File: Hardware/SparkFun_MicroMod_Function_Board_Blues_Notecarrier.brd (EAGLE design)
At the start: 160 x 100 mm, 3 parts, among them J1 MICROMOD_FUNCTION_STANDARD, U1 NOTECARD

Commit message: Board nearly complete, nearing readiness for design review.
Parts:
- added ANT_PWR, WP: JUMPER-SMT_2_NO_SILK, SparkFun-Jumpers:SMT-JUMPER_2_NO_SILK
- added AUX_EN_LED, USB_SHLD, VIO_LED, VMODEM_LED: JUMPER-SMT_2_NC_TRACE_SILK, SparkFun-Jumpers:SMT-JUMPER_2_NC_TRACE_SILK
- added C1, C5, C6, C7: 0.1uF, SparkFun-Capacitors:0402-TIGHT
- added C2: 10uF, SparkFun-Capacitors:0805
- added C3, C4: 100uF, SparkFun-Capacitors:PANASONIC_D
- added C8: 1.0uF, SparkFun-Capacitors:0402-TIGHT
- added D1, D2: RED, SparkFun-LED:LED-0603
- added D3: BLUE, SparkFun-LED:LED-0603
- added D4: PRTR5V0U2F, SparkFun-IC-Power:SOT886
- added D5, D6: 3A/10V/280mV, SparkFun-DiscreteSemi:SOD-323
- added D7: 0.5A/40V/420mV, SparkFun-DiscreteSemi:SOD-323
- added FD1, FD2, FD3, FD4: FIDUCIALUFIDUCIAL, SparkFun-Aesthetics:FIDUCIAL-MICRO
- added H1: STAND-OFF-REFLOW-M2.5_2.5MM_TALL, SparkFun-Hardware:STAND-OFF-REFLOW-M2.5
- added J2: MICROMOD_FUNCTION_STANDARD, SparkFun-MicroMod:M.2-CARD-E-22_FUNCTION_STANDARD
- added J3: (no value), SparkFun-Connectors:1X01_NO_SILK
- added J4: (no value), SparkFun-Connectors:1X07_NO_SILK
- added J5: (no value), SparkFun-Connectors:NANO_SIM_MOLEX_104224-0820
- added J6: NOTECARD, SparkFun_MicroMod_Function_Board_Blues_Notecarrier:M.2-CONNECTOR-E
- added LOGO1: SFE_LOGO_NAME_FLAME.1_INCH, SparkFun-Aesthetics:SFE_LOGO_NAME_FLAME_.1
- added LOGO2: SPECIAL_INSTRUCTIONS-ORDERING, SparkFun-Aesthetics:ORDERING_INSTRUCTIONS
- added LOGO3: OSHW-LOGOMINI, SparkFun-Aesthetics:OSHW-LOGO-MINI
- added MEAS: JUMPER-COMBO_2_NC_TRACE, SparkFun-Jumpers:COMBO-JUMPER_2_NC_TRACE
- added Q1, Q3: 5.8A/30V/35mΩ, SparkFun-DiscreteSemi:SOT23-3
- added Q2, Q4: 20V/4.2A/52mΩ/1.4W, SparkFun-DiscreteSemi:SOT23-3
- added R1, R2: 1k, SparkFun-Resistors:0402-TIGHT
- added R10, R11, R13, R5, R7, R9: 10k, SparkFun-Resistors:0402-TIGHT
- added R12: 2.2M, SparkFun-Resistors:0402-TIGHT
- added R3, R4: 5.1k, SparkFun-Resistors:0402-TIGHT
- added R6: 4.7k, SparkFun-Resistors:0402-TIGHT
- added R8: 560Ω, SparkFun-Resistors:0402-TIGHT
- added S1: MOMENTARY-SWITCH-SPST-SMD-4.6X2.8MM, SparkFun-Switches:TACTILE_SWITCH_SMD_4.6X2.8MM
- added U$1: (no value), output:AEN1
- added U$10: (no value), output:#_AUX3#MCU_#BOOT##0
- added U$11: (no value), output:#_AUX2#0
- added U$12: (no value), output:#_MCU_#DFU_STAT##0
- added U$13: (no value), output:#_AUX_EN#0
- added U$14: (no value), SparkFun-Aesthetics:SFE_LOGO_NAME_FLAME_.1
- added U$15: (no value), output:BLUES_WIRELESS_NOTECARRIER1
- added U$2: (no value), output:VIN3
- added U$3: (no value), output:VIO4
- added U$4: (no value), output:##RESET_##6
- added U$5: (no value), output:##RESET##9
- added U$6: (no value), SparkFun-Aesthetics:SFE_LOGO_FLAME_STOP_.1
- added U$7: (no value), output:#_GND_#0
- added U$8: (no value), output:#_AUX5#0
- added U$9: (no value), output:#_AUX4#MCU_#RST##0
- added U2: TCR2EF33, SparkFun_MicroMod_Function_Board_Blues_Notecarrier:SOT23-5
- J1: value MICROMOD_FUNCTION_STANDARD -> (none); device SparkFun-MicroMod:M.2-CARD-E-22_FUNCTION_STANDARD -> SparkFun-Connectors:USB-C-16P-2LAYER-PADS
- U1: value NOTECARD -> EEPROM; device SparkFun_MicroMod_Function_Board_Blues_Notecarrier:M.2-CONNECTOR-E -> SparkFun-IC-Memory:SO08
- moved J1 108.2 mm to (30.0, 58.9), turned to 180 degrees
- moved U1 55.2 mm to (34.0, 8.70)
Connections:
- new net !RESET!: J3.1, J6.67, S1.3, S1.4
- new net 3.3V: C1.1, C7.1, D1.A, D7.C, J6.2, J6.4, Q2.3, R10.1, R5.1, U1.8
- new net 3V3_IN: J2.73, Q2.2, R7.1, R9.2
- new net A0: J2.36, U1.1
- new net A1: J2.34, U1.2
- new net A2: J2.32, U1.3
- new net ATTN: J2.53, J6.54
- new net AUX1/MCU_!DFU_STAT!: J2.10, J4.6, J6.46
- new net AUX2: J2.57, J4.5, J6.48
- new net AUX3/MCU_!BOOT!: J2.66, J4.4, J6.50
- new net AUX4/MCU_!RST!: J2.68, J4.3, J6.52
- new net AUX5: J2.59, J4.7, J6.38
- new net AUX_EN: D3.A, J2.55, J4.2, J6.56, R10.2
- new net AUX_RX/MCU_TX: J2.4, J6.58
- new net AUX_TX/MCU_RX: J2.6, J6.60
- new net EWP: J2.40, R5.2, U1.7, WP.2
- new net GND: AUX_EN_LED.1, C1.2, C2.2, C3.-, C4.-, C5.2, C6.2, C7.2, C8.2, D4.2, H1.1, J1.GND, J1.GND2, J2.1, J2.2, J2.33, J2.39, J2.45, J2.75, J2.8, J2.GND1, J2.GND2, J2.GND3, J2.GND4, J2.GND5, J2.GND6, J4.1, J5.G1, J5.G2, J5.G3, J5.G4, J5.S4, J6.11, J6.18, J6.3, J6.33, J6.39, J6.45, J6.5, J6.51, J6.57, J6.6, J6.71, J6.73, Q1.2, Q3.2, R12.1, R3.1, R4.1, S1.1, S1.2, U1.4, U2.2, USB_SHLD.1, VIO_LED.1, VMODEM_LED.1, WP.1
- new net N$1: J2.71, R8.2
- new net N$10: C8.1, D7.A, U2.5
- new net N$11: R2.1, VMODEM_LED.2
- new net N$12: R1.1, VIO_LED.2
- new net N$13: D3.C, R6.2
- new net N$14: AUX_EN_LED.2, R6.1
- new net N$2: Q1.3, Q2.1, R9.1
- new net N$3: Q3.3, Q4.1, R11.1
- new net N$37: D5.C, D6.C, MEAS.1, MEAS.3
- new net N$4: D1.C, R1.2
- new net N$5: R13.1, U2.3
- new net N$6: D2.C, R2.2
- new net N$8: J1.B5, R3.2
- new net N$9: J1.A5, R4.2
- new net NOTECARD_RX: J2.13, J6.62
- new net NOTECARD_TX: J2.15, J6.64
- new net PWR_EN: Q1.1, Q3.1, R7.2, R8.1
- new net SCL: J2.21, J6.40, U1.6
- new net SDA: J2.19, J6.42, U1.5
- new net SHLD: J1.SHLD1, J1.SHLD2, J1.SHLD3, J1.SHLD4, USB_SHLD.2
- new net SIM_CLK: J5.S3, J6.14
- new net SIM_IO: J5.S6, J6.12
- new net SIM_RST: J5.S2, J6.10
- new net SIM_VCC: C2.1, J5.S1, J6.8
- new net USB_IN_N: D4.3, J1.A7, J1.B7
- new net USB_IN_P: D4.1, J1.A6, J1.B6
- new net USB_N: D4.4, J6.9
- new net USB_P: D4.6, J6.7
- new net VACT_GPS_IN: ANT_PWR.2, J6.22
- new net VACT_GPS_OUT: ANT_PWR.1, J6.20
- new net VCC: D6.A, Q4.3
- new net VCC_IN: J2.72, J2.74, Q4.2, R11.2
- new net VIN: C3.+, C4.+, C6.1, D2.A, J6.70, J6.72, J6.74, MEAS.2, MEAS.4, R12.2
- new net V_USB: C5.1, D4.5, D5.A, J1.VBUS1, J1.VBUS2, J6.13, R13.2, U2.1
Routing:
- net AUX_EN: track 0.00 -> 97.7 mm, vias 0 -> 7
- net 3.3V: track 0.00 -> 66.9 mm, vias 0 -> 2
- net AUX5: track 0.00 -> 62.0 mm, vias 0 -> 2
- net VIN: track 0.00 -> 57.2 mm, vias 0 -> 2
- net AUX1/MCU_!DFU_STAT!: track 0.00 -> 57.2 mm, vias 0 -> 1
- net !RESET!: track 0.00 -> 56.1 mm, vias 0 -> 1
- net SIM_RST: track 0.00 -> 55.8 mm, vias 0 -> 2
- net AUX2: track 0.00 -> 53.0 mm, vias 0 -> 2
- net AUX3/MCU_!BOOT!: track 0.00 -> 50.0 mm, vias 0 -> 1
- net SIM_CLK: track 0.00 -> 49.0 mm
- net AUX4/MCU_!RST!: track 0.00 -> 47.3 mm, vias 0 -> 1
- net SIM_IO: track 0.00 -> 46.3 mm
- net USB_N: track 0.00 -> 45.1 mm, vias 0 -> 2
- net USB_P: track 0.00 -> 45.0 mm, vias 0 -> 2
- net SDA: track 0.00 -> 43.7 mm, vias 0 -> 3
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- added copper zone on layer 1, net 3.3V
- added copper zone on layer 1, net GND
- added copper zone on layer 16, net GND
- added copper zone on layer 1, net SHLD
- added copper zone on layer 16, net SHLD
- added copper zone on layer 1, net SIM_VCC
- added copper zone on layer 16, net SIM_VCC
- added copper zone on layer 1, net VCC_IN
- added copper zone on layer 16, net VCC_IN
- added copper zone on layer 1, net VIN
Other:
- board size 160 x 100 mm -> 37.5 x 65 mm
- board text added: "Alex Brudner"
- board text added: "v01"

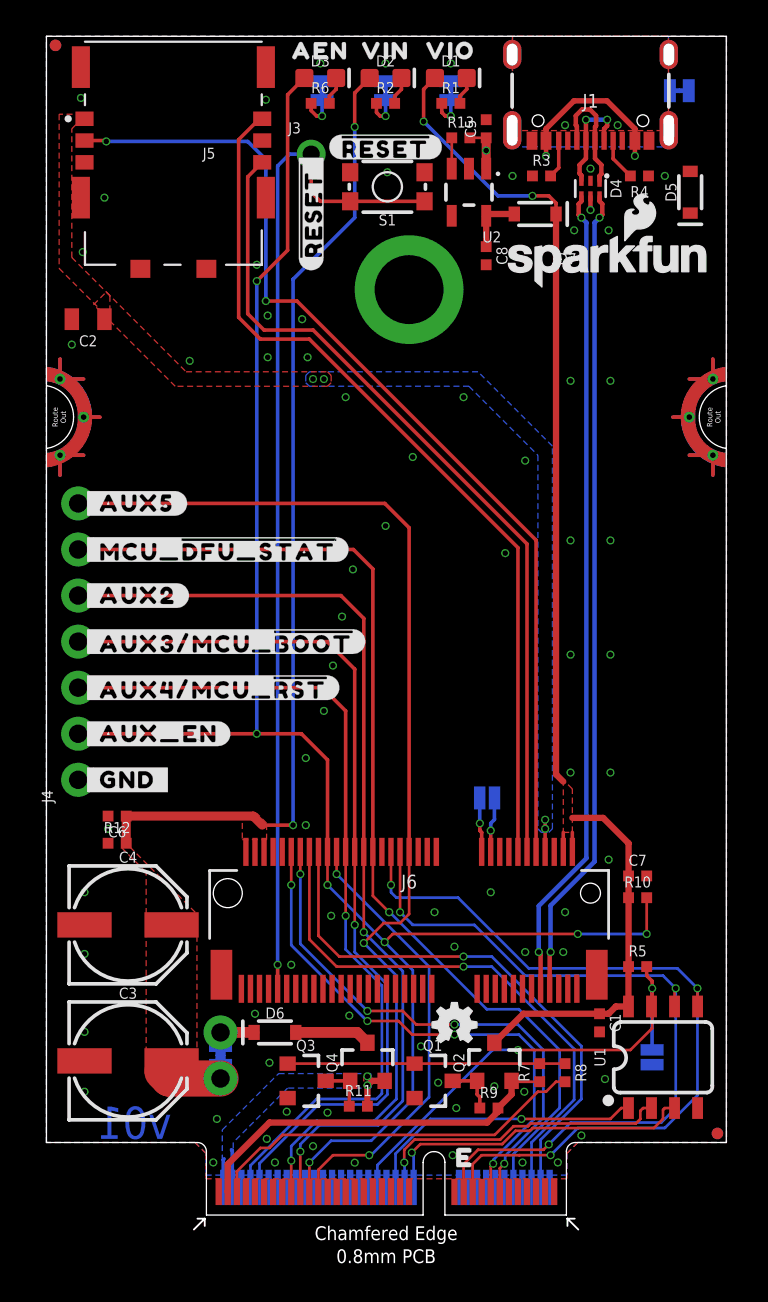
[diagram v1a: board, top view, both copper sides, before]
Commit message: Board routing complete.
Initial routing complete, now finishing silk.
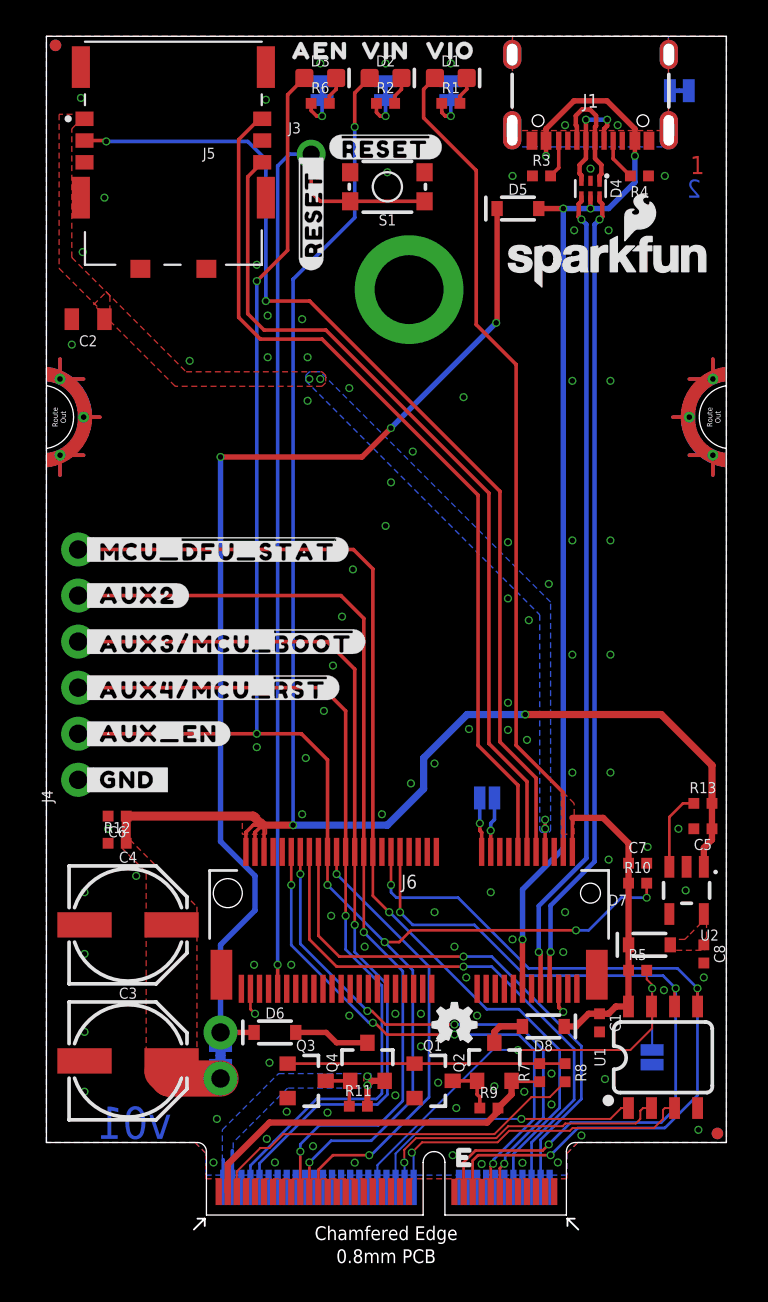
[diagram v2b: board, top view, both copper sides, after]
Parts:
- removed U$8: (no value), output:#_AUX5#0
- added D8: 0.5A/40V/420mV, SparkFun-DiscreteSemi:SOD-323
- J4: device SparkFun-Connectors:1X07_NO_SILK -> SparkFun-Connectors:1X06_NO_SILK
- moved D7 40.8 mm to (33.2, 14.9), turned to 0 degrees
- moved C5 40.4 mm to (36.2, 21.3), turned to 180 degrees
- moved C8 40.3 mm to (36.2, 14.4)
- moved U2 40.3 mm to (35.3, 17.9)
- moved R13 39.1 mm to (36.2, 22.7)
- moved D5 9.54 mm to (26.0, 55.5), turned to 0 degrees
- moved R10 0.80 mm to (32.6, 18.3)
- moved C7 0.70 mm to (32.6, 19.4)
- moved R5 0.20 mm to (32.6, 13.5)
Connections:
- removed net AUX5: J2.59, J4.7, J6.38
- new net N$7: D8.A, Q2.3
- net 3.3V: now also D8.C; no longer Q2.3
- net VIN: now also C5.1, R13.2, U2.1
- net V_USB: no longer C5.1, R13.2, U2.1
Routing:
- net AUX5: track 62.0 -> 0.00 mm, vias 2 -> 0
- net N$37: track 1.85 -> 60.5 mm, vias 0 -> 3
- net V_USB: track 12.5 -> 61.2 mm, vias 4 -> 5
- net VIN: track 57.2 -> 96.8 mm, vias 2 -> 3
- net N$10: track 3.29 -> 0.00 mm
- net GND: track 0.00 -> 2.86 mm, vias 17 -> 105
- net N$5: track 1.70 -> 4.41 mm
- net N$7: track 0.00 -> 2.27 mm
- net 3.3V: track 66.9 -> 64.7 mm, vias 2 -> 0
- added copper zone on layer 1, net N$10
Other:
- board text added: "1"
- board text added: "2"

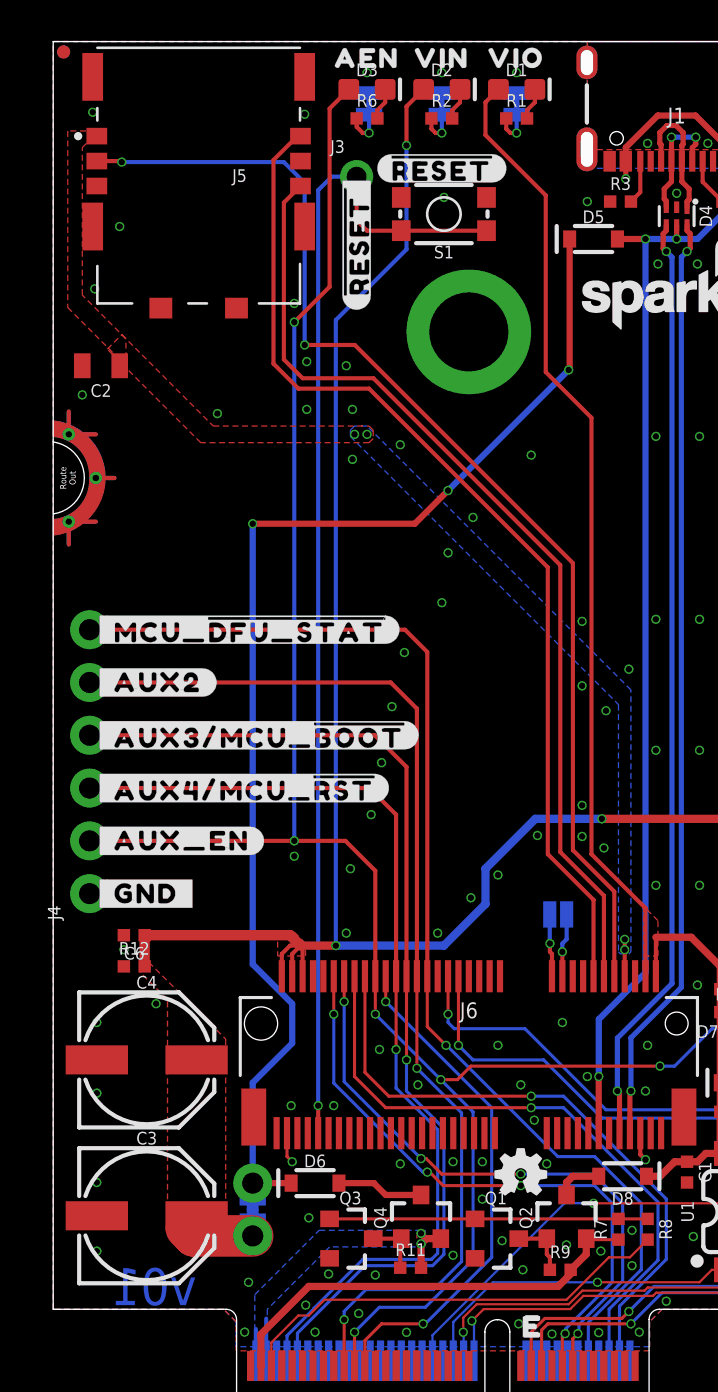
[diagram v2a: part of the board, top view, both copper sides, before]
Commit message: Initial Silk completed.
May add Blues Wireless logo.
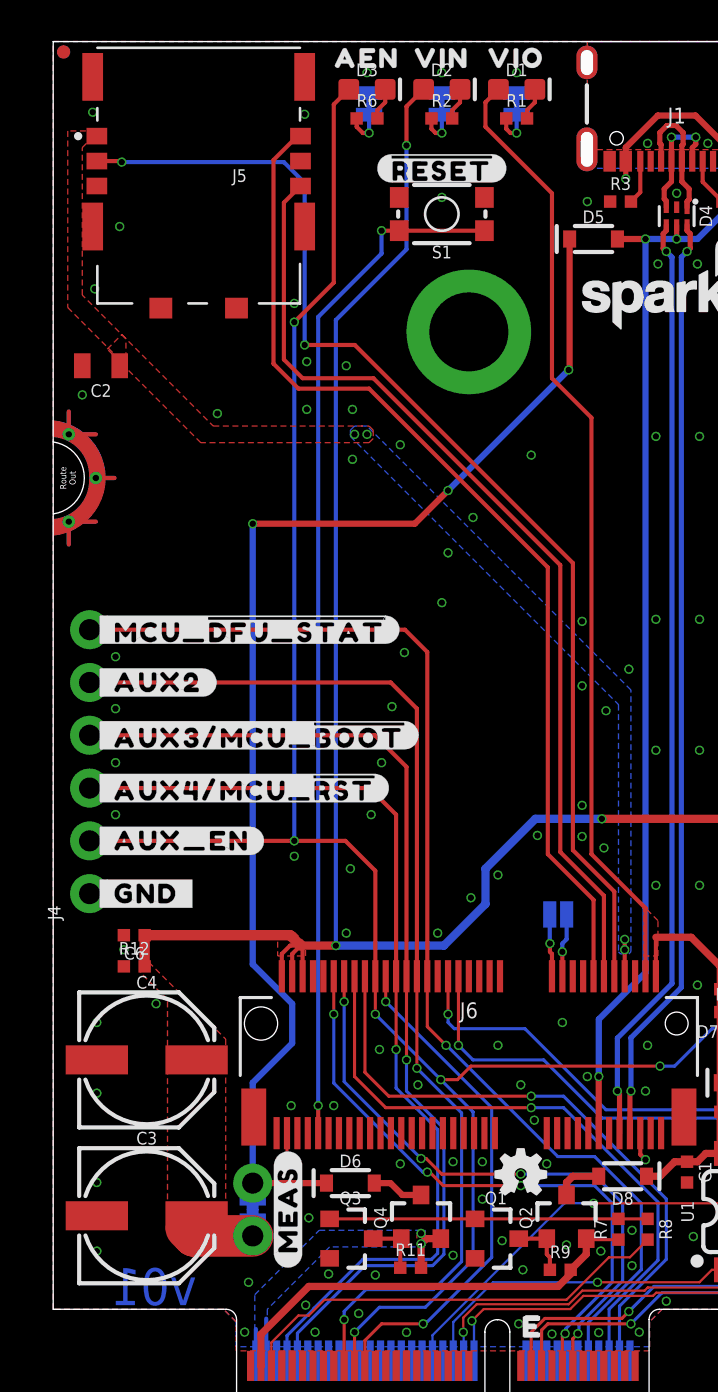
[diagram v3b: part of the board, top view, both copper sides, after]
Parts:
- removed J3: (no value), SparkFun-Connectors:1X01_NO_SILK
- added U$16, U$17: (no value), output:#MEAS#4
- added U$18: (no value), output:#_ANT_PWR#5
- added U$19: (no value), output:#AUX_EN_LED_#20
- added U$20: (no value), output:#_SHLD#23
- added U$21: (no value), output:#PWR_LED_#17
- added U$22: (no value), output:#_GND_#24
- added U$23: (no value), output:#AUX_EN_#25
- added U$24: (no value), output:#AUX4#MCU_#RST##0
- added U$25: (no value), output:#AUX3#MCU_#BOOT##0
- added U$26: (no value), output:#AUX2_#0
- added U$27: (no value), output:#AUX1#MCU_#DFU_STAT##0
- added U$28: (no value), SparkFun-MicroMod:MICROMOD_LOGO_.3
- added U$8: (no value), output:#_WP#2
- U$4: device output:##RESET_##6 -> output:#VIO_LED_#21
- moved U$4 8.10 mm to (22.3, 54.6), flipped to the bottom
- moved U$14 1.77 mm to (20.4, 43.2)
- moved D6 1.70 mm to (14.3, 10.1)
- moved U$15 0.30 mm to (20.0, 39.4)
- moved S1 0.10 mm to (18.7, 56.7)
- renumbered USB_SHLD to SHLD, VMODEM_LED to PWR_LED
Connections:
- net !RESET!: no longer J3.1
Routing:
- net !RESET!: track 56.1 -> 49.6 mm, vias 1 -> 2
- net N$37: track 60.5 -> 62.2 mm
- net VCC: track 4.19 -> 2.49 mm
- net GND: vias 105 -> 109
